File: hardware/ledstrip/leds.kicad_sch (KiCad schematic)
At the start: 5 parts, among them J5 Ledstrip connector, Q1 Q_NMOS, Q11 Q_NMOS, Q2 Q_NMOS, Q3 Q_NMOS

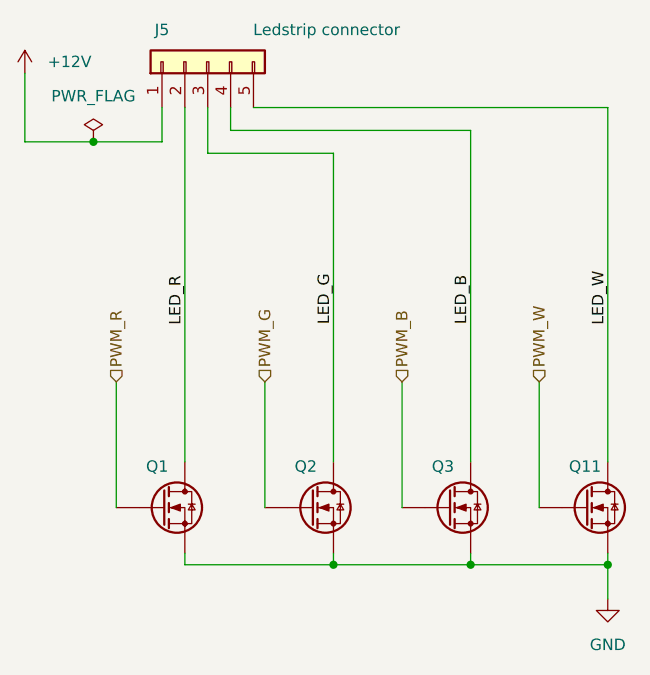
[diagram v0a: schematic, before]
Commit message: Add a lot of TestPoints
Move P-FET at the edge of board.
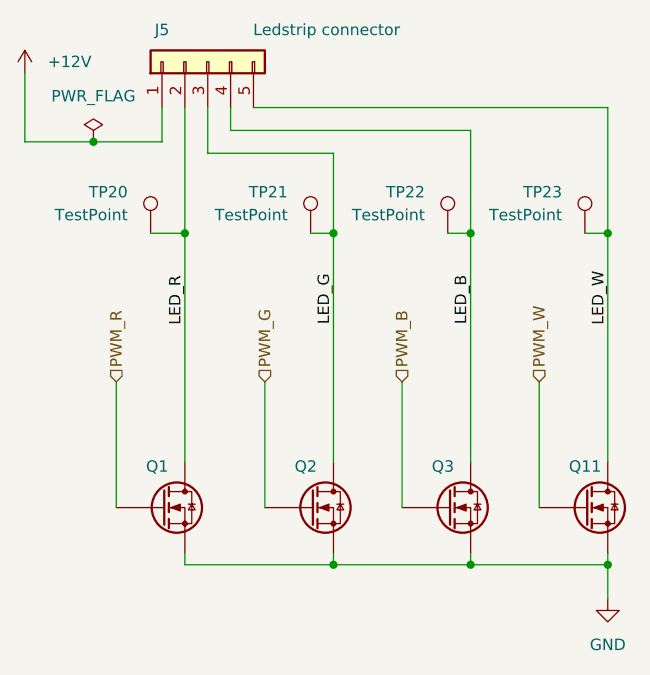
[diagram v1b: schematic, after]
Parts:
- added TP20, TP21, TP22, TP23: TestPoint, TestPoint:TestPoint_Pad_1.0x1.0mm, symbol Connector:TestPoint
- J5: footprint Connector_JST:JST_XH_B5B-XH-A_1x05_P2.50mm_Vertical -> Connector_JST:JST_XH_S5B-XH-A_1x05_P2.50mm_Horizontal; Distributor Link 1 (none) -> https://www.mouser.fr/ProductDetail/JST-Commercial/S5B-XH-A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; MPN (none) -> S5B-XH-A-1(LF)(SN); Manufacturer (none) -> JST
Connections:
- net LED_B: now also TP22.1
- net LED_G: now also TP21.1
- net LED_R: now also TP20.1
- net LED_W: now also TP23.1

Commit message: Improve BOM: exclude uneeded parts, add some columns.
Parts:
- TP20, TP21, TP22, TP23: now left out of the parts list

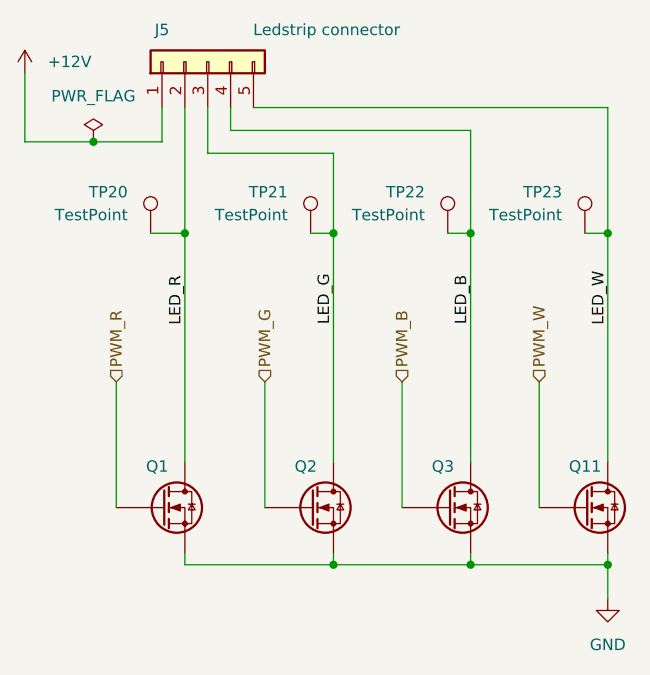
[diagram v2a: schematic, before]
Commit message: Mark through-hole component "Do not place" in schematics.
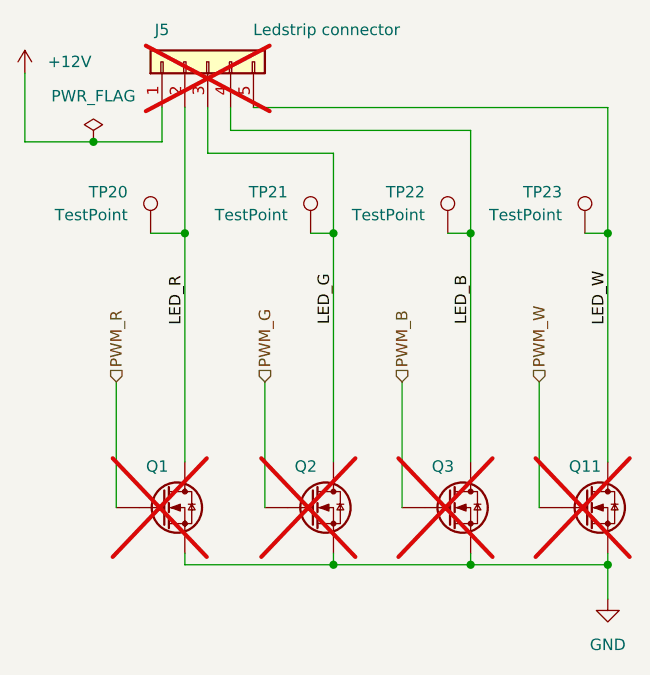
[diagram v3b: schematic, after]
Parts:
- J5, Q1, Q11, Q2, Q3: now not fitted
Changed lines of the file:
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@@
 		(in_bom yes)
 		(on_board yes)
-		(dnp no)
+		(dnp yes)
 		(property "Reference" "Q11"
 			(at 159.512 104.648 0)
@@
 		(in_bom yes)
 		(on_board yes)
-		(dnp no)
+		(dnp yes)
 		(property "Reference" "Q3"
 			(at 144.272 104.648 0)
@@
 		(in_bom yes)
 		(on_board yes)
-		(dnp no)
+		(dnp yes)
 		(property "Reference" "Q1"
 			(at 112.522 104.648 0)
@@
 		(in_bom yes)
 		(on_board yes)
-		(dnp no)
+		(dnp yes)
 		(property "Reference" "Q2"
 			(at 129.032 104.648 0)
@@
 		(in_bom yes)
 		(on_board yes)
-		(dnp no)
+		(dnp yes)
 		(property "Reference" "J5"
 			(at 114.3 56.134 90)
